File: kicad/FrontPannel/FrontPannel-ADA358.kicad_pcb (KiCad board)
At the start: 2 copper layers, 198 x 58 mm, 18 parts

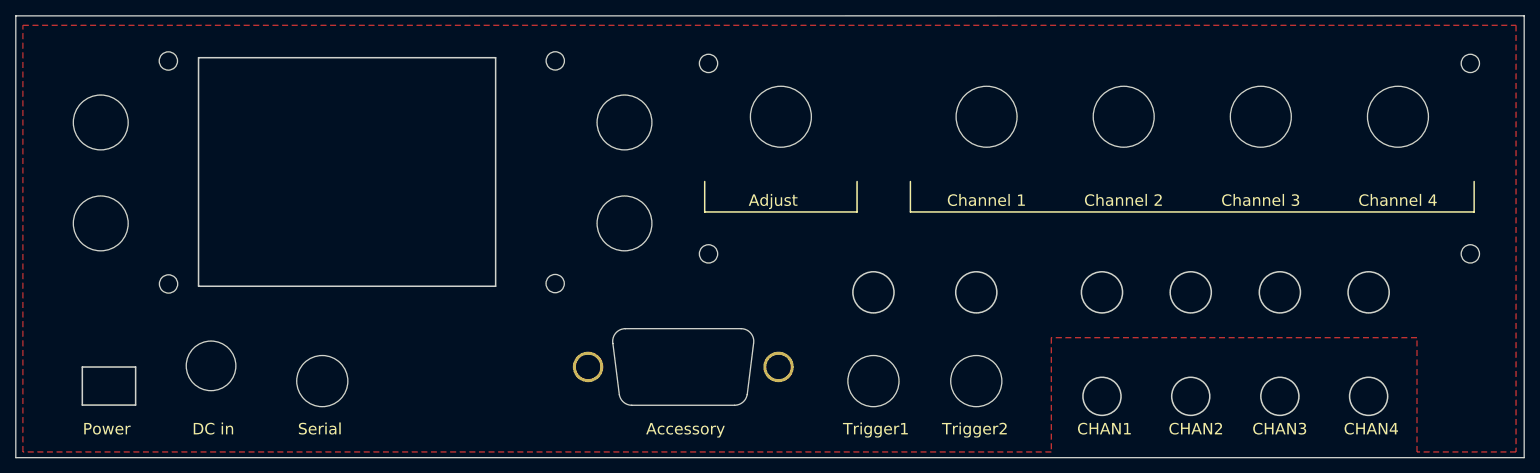
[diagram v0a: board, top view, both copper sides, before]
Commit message: enlarge holes for pots on front panel
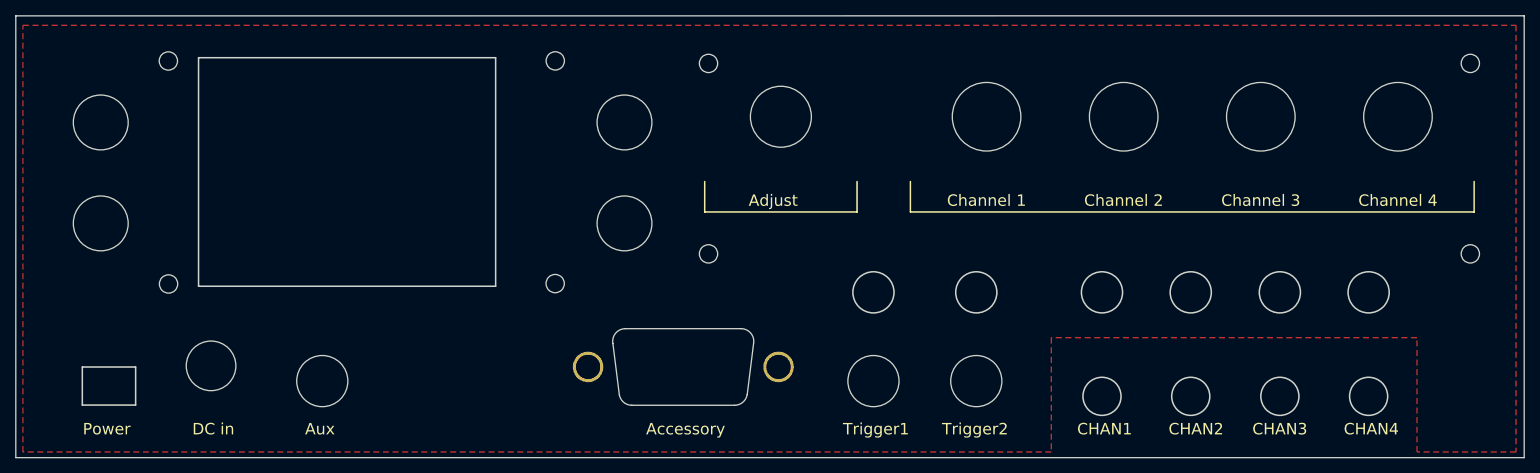
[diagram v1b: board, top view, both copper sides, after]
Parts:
- REF** (x4): value BOURNS PEC11L-4125F-S0020-Panel -> RK09L1140A2U-panel; footprint ProjLib:BOURNS PEC11L-4125F-S0020-Panel -> Library:RK09L1140A2U-panel
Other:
- net class Default removed
- board text added: "Aux"
- board text added: "ZC95 Front panel v0.2"
- board text removed: "Serial"
- board text removed: "ZC95 Front panel v0.1"

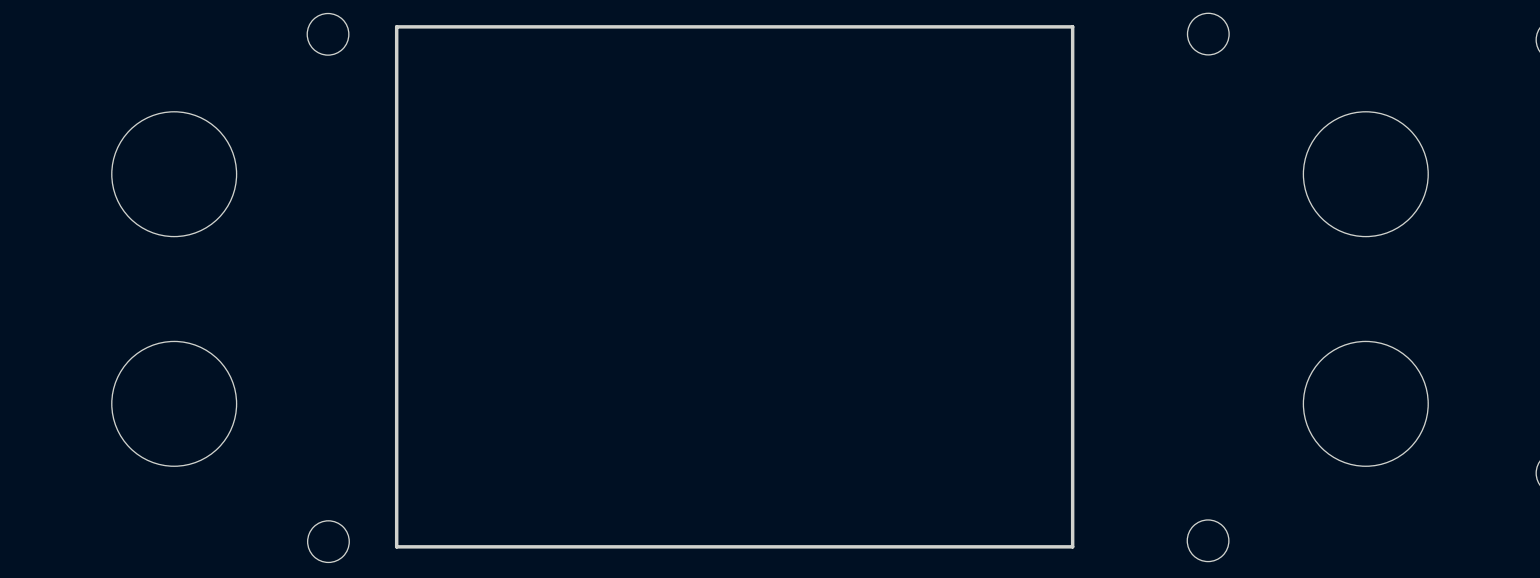
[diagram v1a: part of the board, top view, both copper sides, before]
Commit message: enlarge button holes to 8.1mm for LP1OA1Ax buttons
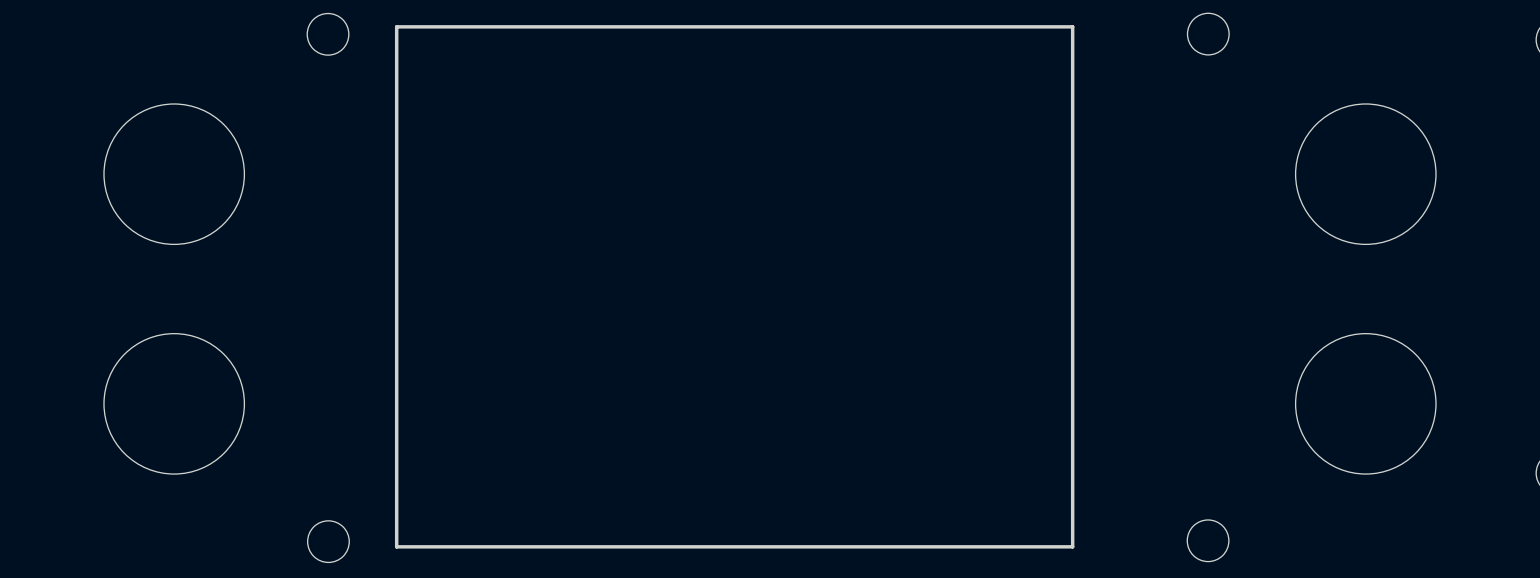
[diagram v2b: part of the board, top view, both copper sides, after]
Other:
- board text added: "ZC95 Front panel v0.3"
- board text removed: "ZC95 Front panel v0.2"
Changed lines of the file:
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@@
     (fp_circle (center 0 0) (end 2.2 0) (layer "Cmts.User") (width 0.15) (fill none))
     (fp_circle (center 0 0) (end 2.45 0) (layer "F.CrtYd") (width 0.05) (fill none))
-    (pad "" np_thru_hole circle locked (at 0 0) (size 7.2 7.2) (drill 7.2) (layers *.Cu *.Mask))
+    (pad "" np_thru_hole circle locked (at 0 0) (size 8.1 8.1) (drill 8.1) (layers F&B.Cu *.Mask))
   )
   (footprint "MountingHole:MountingHole_2.2mm_M2" (layer "F.Cu")
@@
     (fp_circle (center 0 0) (end 2.2 0) (layer "Cmts.User") (width 0.15) (fill none))
     (fp_circle (center 0 0) (end 2.45 0) (layer "F.CrtYd") (width 0.05) (fill none))
-    (pad "" np_thru_hole circle locked (at 0 0) (size 7.2 7.2) (drill 7.2) (layers *.Cu *.Mask))
+    (pad "" np_thru_hole circle locked (at 0 0) (size 8.1 8.1) (drill 8.1) (layers F&B.Cu *.Mask))
   )
   (footprint "MountingHole:MountingHole_2.2mm_M2" (layer "F.Cu")
@@
     (fp_line (start -3.05 -9.1) (end 12.15 -9.1) (layer "Edge.Cuts") (width 0.12))
     (fp_line (start 13.78204 -7.13232) (end 12.95 -0.45) (layer "Edge.Cuts") (width 0.12))
-    (fp_arc (start -2.2 0.95) (mid -3.267027 0.561634) (end -3.834781 -0.421744) (layer "Edge.Cuts") (width 0.12))
+    (fp_arc (start -2.2 0.95) (mid -3.267028 0.561634) (end -3.834781 -0.421744) (layer "Edge.Cuts") (width 0.12))
     (fp_arc (start -4.684781 -7.151744) (mid -4.321634 -8.507028) (end -3.05 -9.1) (layer "Edge.Cuts") (width 0.12))
     (fp_arc (start 12.934781 -0.421744) (mid 12.367028 0.561634) (end 11.3 0.95) (layer "Edge.Cuts") (width 0.12))
@@
     (fp_circle (center 0 0) (end 2.2 0) (layer "Cmts.User") (width 0.15) (fill none))
     (fp_circle (center 0 0) (end 2.45 0) (layer "F.CrtYd") (width 0.05) (fill none))
-    (pad "" np_thru_hole circle locked (at 0 0) (size 7.2 7.2) (drill 7.2) (layers *.Cu *.Mask))
+    (pad "" np_thru_hole circle locked (at 0 0) (size 8.1 8.1) (drill 8.1) (layers F&B.Cu *.Mask))
   )
   (footprint "MountingHole:MountingHole_2.2mm_M2" (layer "F.Cu")
@@
     (fp_circle (center 0 0) (end 2.2 0) (layer "Cmts.User") (width 0.15) (fill none))
     (fp_circle (center 0 0) (end 2.45 0) (layer "F.CrtYd") (width 0.05) (fill none))
-    (pad "" np_thru_hole circle locked (at 0 0) (size 7.2 7.2) (drill 7.2) (layers *.Cu *.Mask))
+    (pad "" np_thru_hole circle locked (at 0 0) (size 8.1 8.1) (drill 8.1) (layers F&B.Cu *.Mask))
   )
   (footprint "MountingHole:MountingHole_2.2mm_M2" (layer "F.Cu")
@@
     (effects (font (size 1.5 1.5) (thickness 0.3)))
   )
-  (gr_text "ZC95 \nFront panel\nv0.2" (at 157 116.5) (layer "B.SilkS")
+  (gr_text "ZC95 \nFront panel\nv0.3" (at 157 116.5) (layer "B.SilkS")
     (effects (font (size 1.5 1.5) (thickness 0.3)) (justify mirror))
   )
